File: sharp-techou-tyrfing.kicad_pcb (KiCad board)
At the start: 2 copper layers, 81 x 118.2 mm, 3 parts, among them J1 PDA, J2 Breakout, J3 Cartridge

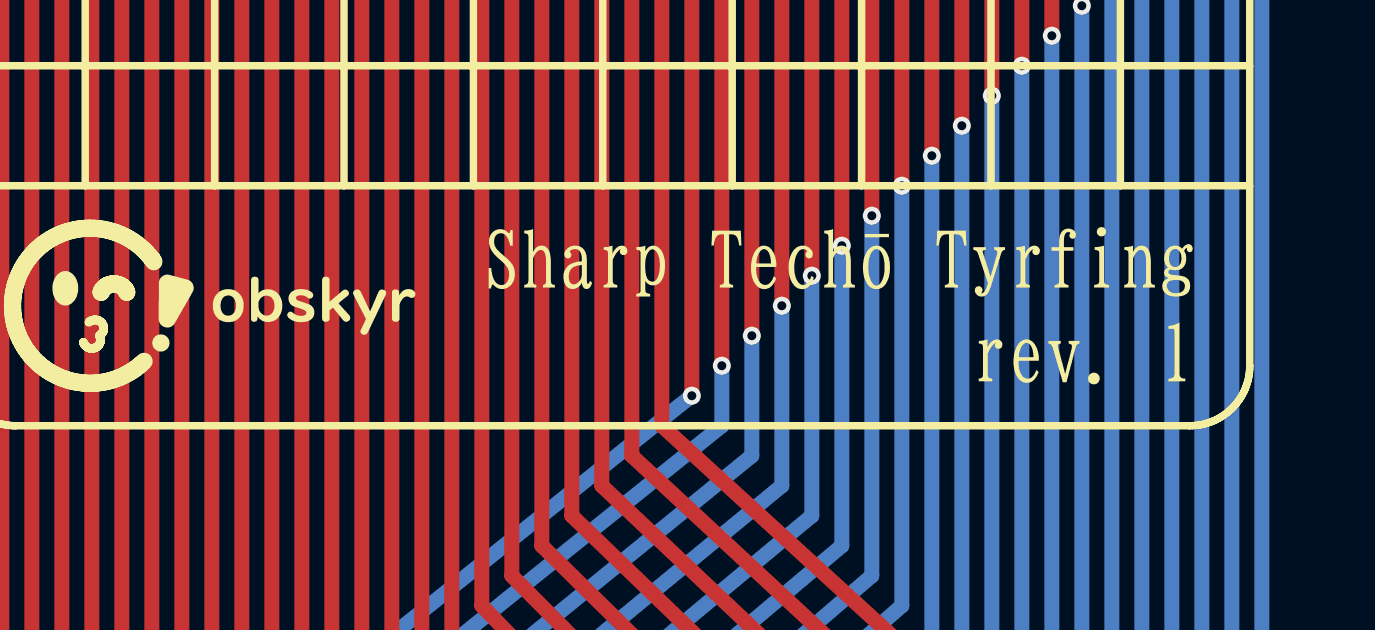
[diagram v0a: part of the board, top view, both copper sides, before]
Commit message: Added Open Source Hardware logo; moved name and revision to a text element.
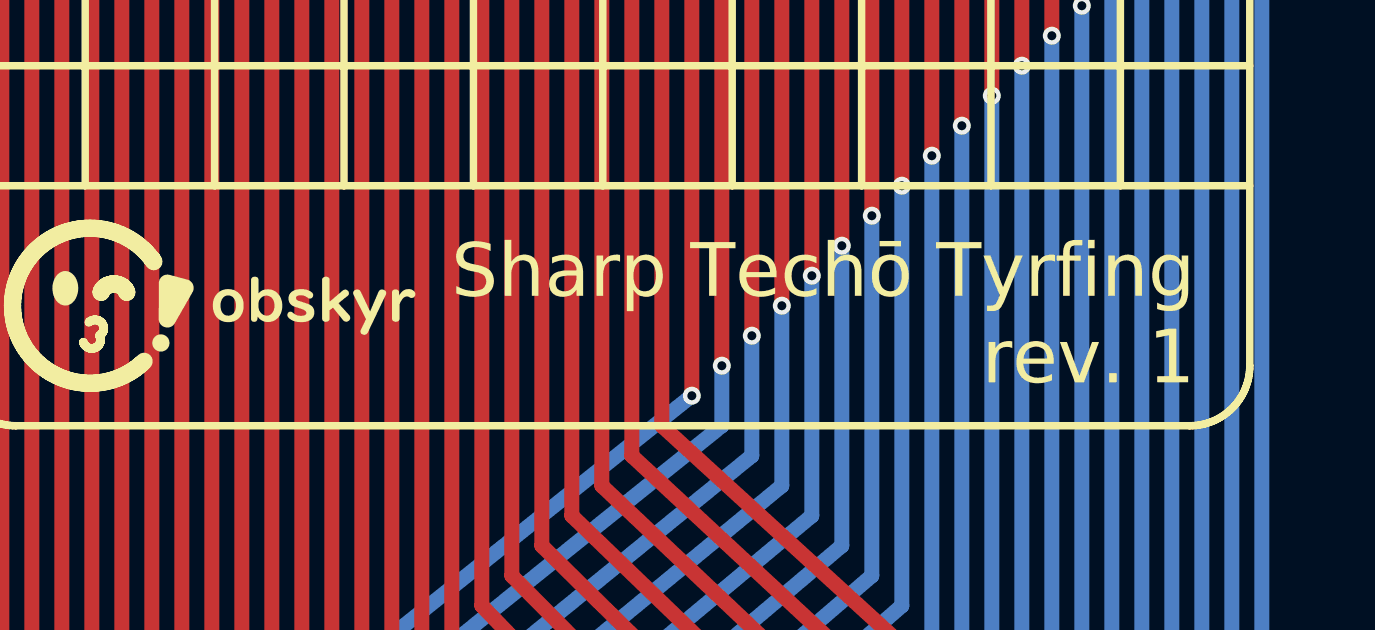
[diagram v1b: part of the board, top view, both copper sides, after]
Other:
- board text added: "Sharp Techō Tyrfing rev. 1"
- board text added: "github.com/obskyr/sharp-techou-tyrfing"
